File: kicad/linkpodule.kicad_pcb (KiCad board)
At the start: 2 copper layers, 160 x 100 mm, 25 parts, among them IC1 74HCT245, IC2 74HCT245, IC3 N82S123AN, IC4 PAL16L8-25, IC5A1 IMSC011, IC5B1 IMSC012, IC6 5MHZ, IC7 74HCT175, IC8 74HCT244, J1 DIN41612_02x32_AC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

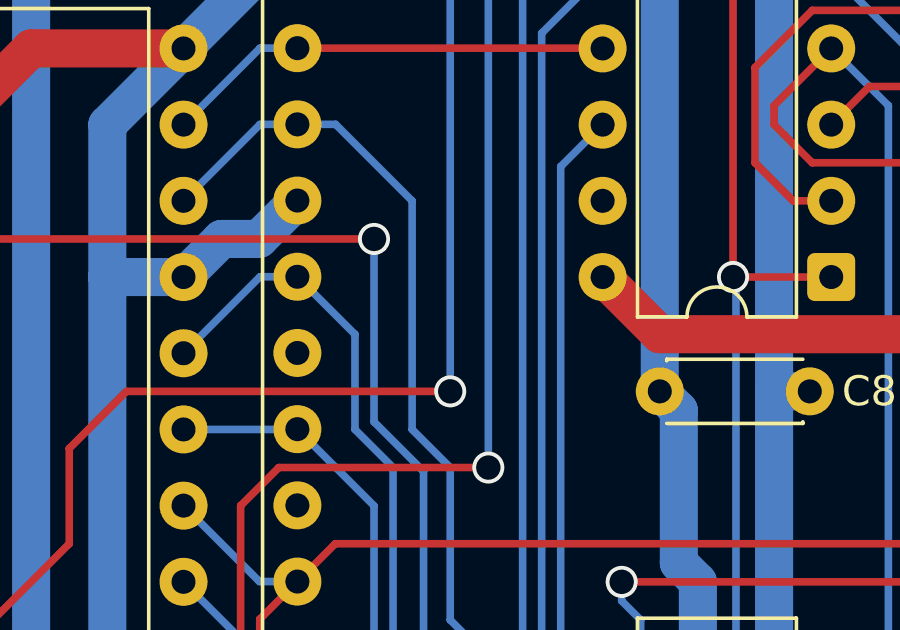
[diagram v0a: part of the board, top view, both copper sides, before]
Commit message: kicad: Add missing D3 connection on PAL
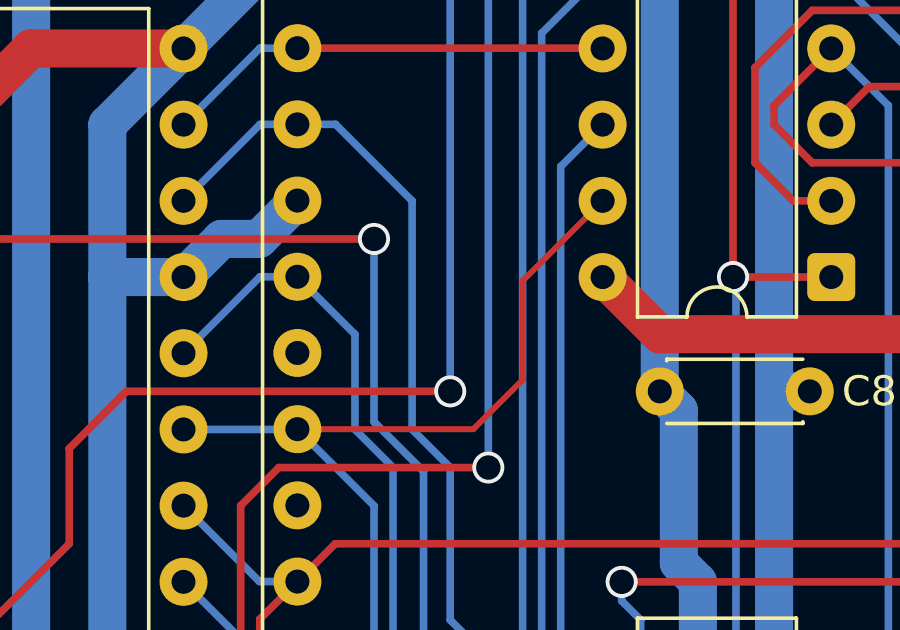
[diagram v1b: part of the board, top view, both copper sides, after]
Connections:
- IC4 pad 19: unconnected-(IC4-~{O_{8}}-Pad19) -> /B_BD3
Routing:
- net /B_BD3: track 105.5 -> 120.8 mm
